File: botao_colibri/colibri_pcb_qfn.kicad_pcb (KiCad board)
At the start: 2 copper layers, 72.5 x 47.1 mm, 39 parts, among them J1 USB4970-00-A_REVA, J2 TC2030, J3 Conn_01x02, J4 PJ-307C, SW1 B3F-3122, U1 ME54BS12, U4 NPM1300-QEAA-R7

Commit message: mudanças nas trilhas
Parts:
- moved R5 0.13 mm to (145.7, 94.6)
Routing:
- net GND: track 124.6 -> 184.5 mm
- net P2_SQUARE_WAVE: track 0.00 -> 18.3 mm
- net USB.VBUS: track 5.85 -> 21.6 mm
- net P2_SENSE: track 0.00 -> 15.3 mm
- net USB.CC1: track 0.00 -> 9.72 mm
- net USB.CC2: track 0.00 -> 9.51 mm
- net BTN_PWR: track 35.3 -> 37.6 mm
- net NPM1300_EN: track 67.2 -> 69.3 mm
- net NPM1300_INT: track 73.3 -> 74.6 mm
- net VDD: track 129.6 -> 130.7 mm
- net I2C_SCL: track 87.5 -> 88.2 mm

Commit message: Desenho dos pads do botão principal, GPIOS acessíveis (adição de conectores para as GPIOS sem uso atual), retrabalho de trilhas.
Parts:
- added J5: Conn_01x06, Connector_PinHeader_2.54mm:PinHeader_1x06_P2.54mm_Vertical, F.Cu at (128.3, 114.3)
- added J6: Conn_01x06, Connector_PinHeader_2.54mm:PinHeader_1x06_P2.54mm_Vertical, F.Cu at (128.3, 110.8)
- added J7: Conn_01x06, Connector_PinHeader_2.54mm:PinHeader_1x06_P2.54mm_Vertical, F.Cu at (128.3, 107.2)
- added sw_principal1: SW_Push, botao_colibri:sw_principal, F.Cu at (159.8, 79.5)
- moved J2 3.85 mm to (149.7, 78.8)
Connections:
- U1 pad 12: unconnected-(U1-P0.00-Pad12) -> P0.00
- U1 pad 7: unconnected-(U1-P1.02/NFC1-Pad7) -> P1.02
- U1 pad A6: unconnected-(U1-P0.04-PadA6) -> P0.04
- U1 pad B1: unconnected-(U1-P1.09-PadB1) -> P1.09
- U1 pad B6: unconnected-(U1-P2.09-PadB6) -> P2.09
- U1 pad C1: unconnected-(U1-P1.10-PadC1) -> P1.10
- U1 pad C6: unconnected-(U1-P2.10-PadC6) -> P2.10
- U1 pad D1: unconnected-(U1-P2.00-PadD1) -> P2.00
- U1 pad D5: unconnected-(U1-P2.08-PadD5) -> P2.08
- U1 pad D6: unconnected-(U1-P2.07-PadD6) -> P2.07
- U1 pad E1: unconnected-(U1-P1.08-PadE1) -> P1.08
- U1 pad E5: unconnected-(U1-P2.05-PadE5) -> P2.05
- U1 pad E6: unconnected-(U1-P2.06-PadE6) -> P2.06
- U1 pad F1: unconnected-(U1-P1.07/AIN3-PadF1) -> P1.07
- U1 pad F3: unconnected-(U1-P2.01-PadF3) -> P2.01
- U1 pad F4: unconnected-(U1-P2.03-PadF4) -> P2.03
- U1 pad F5: unconnected-(U1-P2.02-PadF5) -> P2.02
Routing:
- net P2_SQUARE_WAVE: track 18.3 -> 64.2 mm, vias 0 -> 2
- net GND: track 184.5 -> 230.1 mm, vias 0 -> 2
- net NPM1300_INT: track 74.6 -> 107.0 mm, vias 2 -> 4
- net NPM1300_EN: track 69.3 -> 82.3 mm, vias 2 -> 4
- net SWCLK: track 30.2 -> 24.6 mm
- net VDD: track 130.7 -> 136.0 mm
- net VDDA: track 3.78 -> 8.47 mm
- net NRESET: track 23.0 -> 19.0 mm
- net SWDIO: track 26.9 -> 23.2 mm

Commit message: continuação
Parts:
- removed J7: Conn_01x06, Connector_PinHeader_2.54mm:PinHeader_1x06_P2.54mm_Vertical
- added -: TestPoint, TestPoint:TestPoint_Pad_D1.0mm, F.Cu at (194.5, 108.2)
- moved VBATT_TP1 4.43 mm to (191.2, 111.4)
- moved J6 0.97 mm to (128.1, 109.8)
- moved J5 0.69 mm to (128.1, 113.7)
- renumbered J3 to +
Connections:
- J5 pad 1: GND -> P2.01
- J5 pad 2: P1.07 -> P2.03
- J5 pad 3: P1.02 -> P2.02
- J5 pad 4: P1.08 -> P2.05
- J5 pad 5: P1.09 -> P2.08
- J5 pad 6: P1.10 -> P2.06
- J6 pad 1: P0.00 -> P1.02
- J6 pad 2: P0.04 -> P1.09
- J6 pad 3: P2.00 -> P1.10
- J6 pad 4: P2.01 -> P2.00
- J6 pad 5: P2.02 -> P1.08
- J6 pad 6: P2.03 -> P1.07
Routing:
- net P2.06: track 0.00 -> 76.6 mm, vias 0 -> 2
- net P2.08: track 0.00 -> 61.7 mm, vias 0 -> 2
- net P2.05: track 0.00 -> 59.1 mm, vias 0 -> 2
- net P2.02: track 0.00 -> 52.9 mm, vias 0 -> 2
- net P2.03: track 0.00 -> 52.3 mm, vias 0 -> 2
- net P1.07: track 0.00 -> 42.2 mm
- net P2.01: track 0.00 -> 38.4 mm, vias 0 -> 2
- net P1.02: track 0.00 -> 31.9 mm
- net P2.00: track 0.00 -> 27.3 mm
- net P1.10: track 0.00 -> 25.2 mm
- net P1.09: track 0.00 -> 23.5 mm
- net P1.08: track 0.00 -> 21.9 mm
- net P2_SQUARE_WAVE: track 64.2 -> 81.8 mm
- net NPM1300_INT: track 107.0 -> 90.1 mm, vias 4 -> 6
- net GND: track 230.1 -> 238.9 mm
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
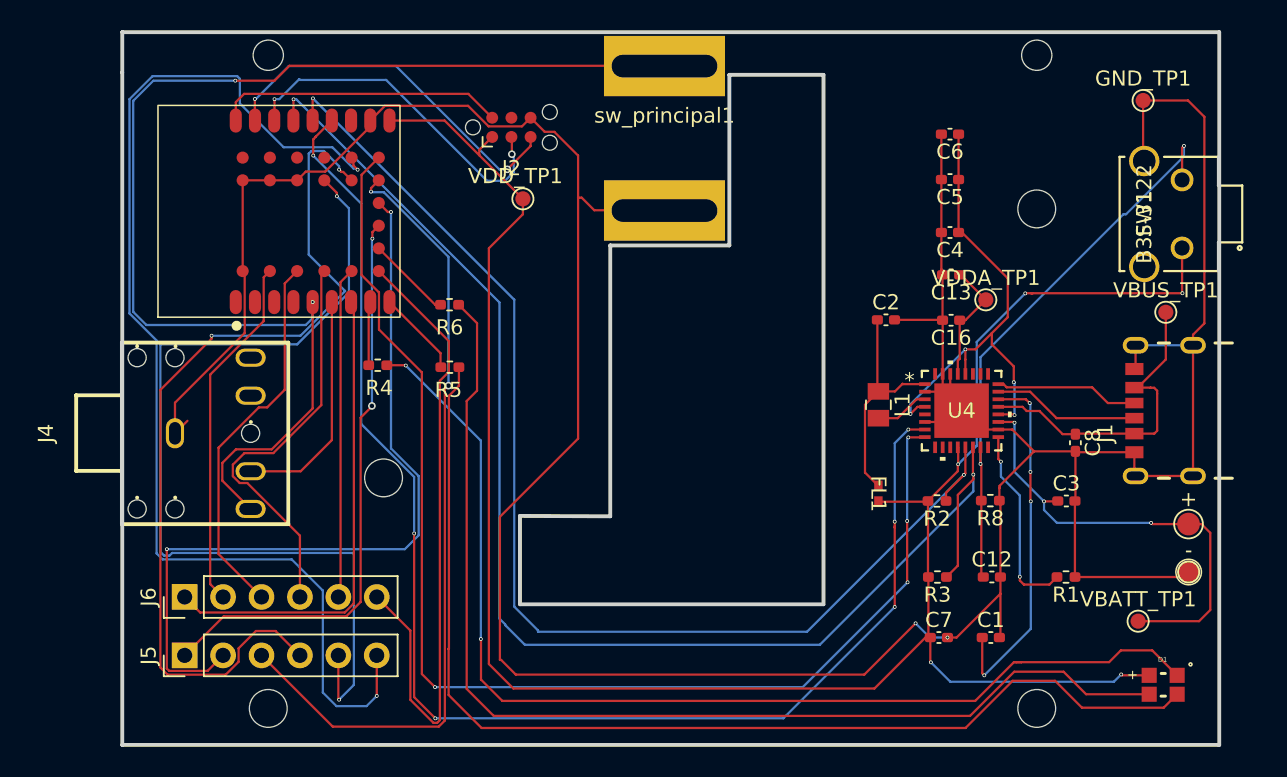
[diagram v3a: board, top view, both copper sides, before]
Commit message: Mudanças de posição de componentes e trilhas
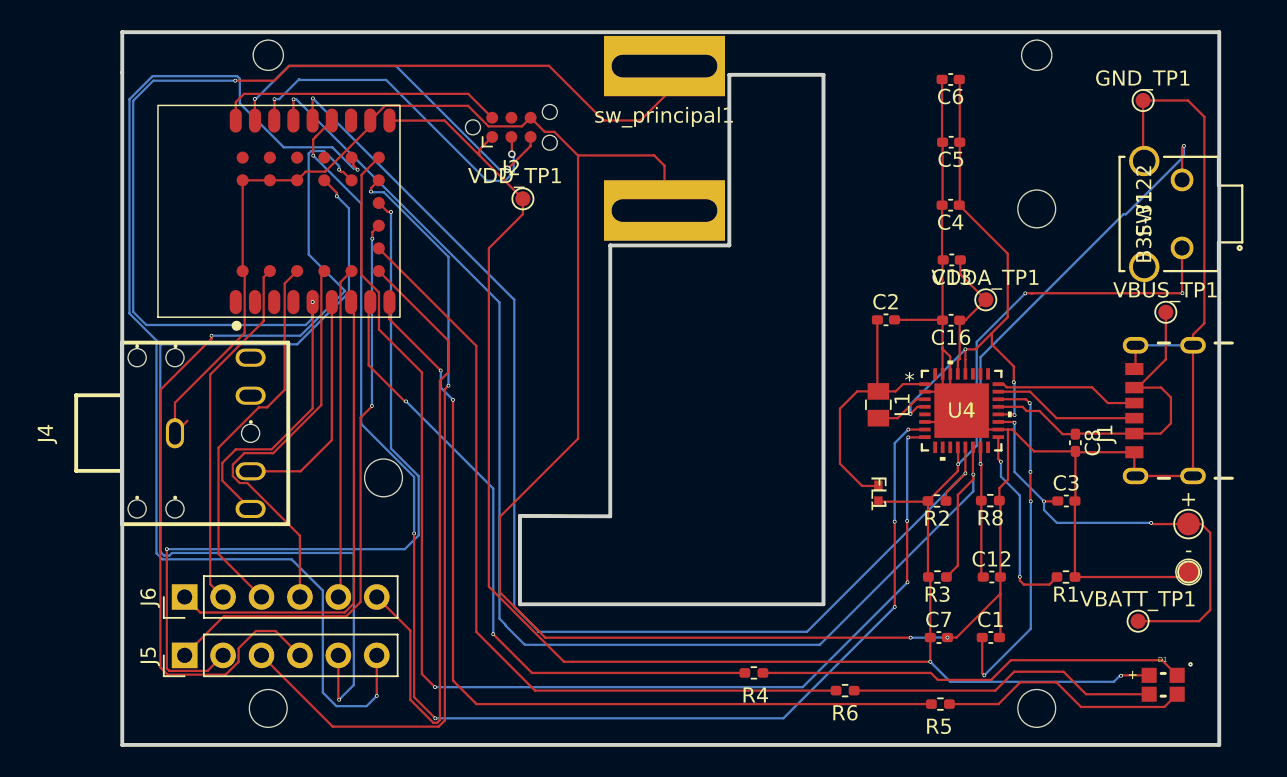
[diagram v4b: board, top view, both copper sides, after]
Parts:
- moved R5 39.3 mm to (178.1, 116.9)
- moved R6 36.5 mm to (171.8, 116.0)
- moved R4 32.1 mm to (165.8, 114.8)
- moved C6 3.62 mm to (178.8, 75.6)
- moved C5 2.47 mm to (178.8, 79.8)
- moved C4 1.81 mm to (178.8, 83.9)
- moved C13 0.99 mm to (178.8, 87.5)
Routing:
- net Net-(D1-Pad2): track 73.4 -> 16.7 mm
- net LED_G: track 5.57 -> 59.0 mm, vias 0 -> 2
- net Net-(D1-Pad3): track 73.9 -> 20.6 mm
- net LED_B: track 5.62 -> 53.4 mm
- net Net-(D1-Pad1): track 73.2 -> 28.5 mm, vias 2 -> 0
- net LED_R: track 4.22 -> 43.2 mm, vias 0 -> 2
- net VDD: track 136.0 -> 131.0 mm
- net P2_SQUARE_WAVE: track 81.8 -> 86.0 mm
- net PVDD: track 32.9 -> 36.4 mm
- net GND: track 238.9 -> 242.4 mm
- net Net-(U4-VOUT1): track 15.0 -> 17.8 mm
- net USB.VBUS: track 21.6 -> 22.8 mm
- net VDDA: track 8.47 -> 9.47 mm
